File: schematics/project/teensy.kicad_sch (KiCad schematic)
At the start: 1 part

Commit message: First steps with kicad structure -> kinda sucks
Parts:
- added D? (x2): US1G, Diode_SMD:D_SMA, symbol Diode:US1G
- gave numbers to parts that had none: 1
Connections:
- net GND: now reaches U1.1 (GND)
- net GND: now also U1.64 (GND)
- net CS: now reaches U1.12 (10_CS_MQSR)
- net MOSI: now reaches U1.13 (11_MOSI_CTX1)
- net MISO: now reaches U1.14 (12_MISO_MQSL)
- net SCK: now reaches U1.35 (13_SCK_LED)
- net IRQ: now reaches U1.4 (2_OUT2)
- net SDA: now reaches U1.40 (18_A4_SDA)
- net SCL: now reaches U1.41 (19_A5_SCL)
- net +3V3: now reaches U1.46 (3V3)
- net +5P: now reaches U1.48 (VIN)
- net +5P: now also D?.2 (A)
- net +5F: now reaches U1.49 (VUSB)
- net +5F: now also D?.2 (A)
- new net +5V: D?.1 (K), D?.1 (K)
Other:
- note added: "IRQ geht auf OUT2????"
- note added: "MEM_CS von prop shield geht auf OUT1D???"

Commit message: some progress, dust slowly clears
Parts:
- removed D? (x2): US1G, Diode_SMD:D_SMA, symbol Diode:US1G
- added D1, D2: PMEG40T20ER, Diode_SMD:Nexperia_CFP3_SOD-123W, symbol Diode:PMEG40T20ER
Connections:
- net +5F: now also D1.2 (A)
- net +5P: now also D2.2 (A)
- net +5V: now also D1.1 (K), D2.1 (K)
- net footpad_a : now reaches U1.36 (14_A0_TX3_SPDIF_OUT)
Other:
- note added: "USB"

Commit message: small progress, angsthasen
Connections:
- net +3V3: now also U1.15 (3V3)
- net GND: now also U1.34 (GND), U1.47 (GND), U1.52 (GND), U1.58 (GND), U1.59 (GND)
- no-connect marks 0 -> 2

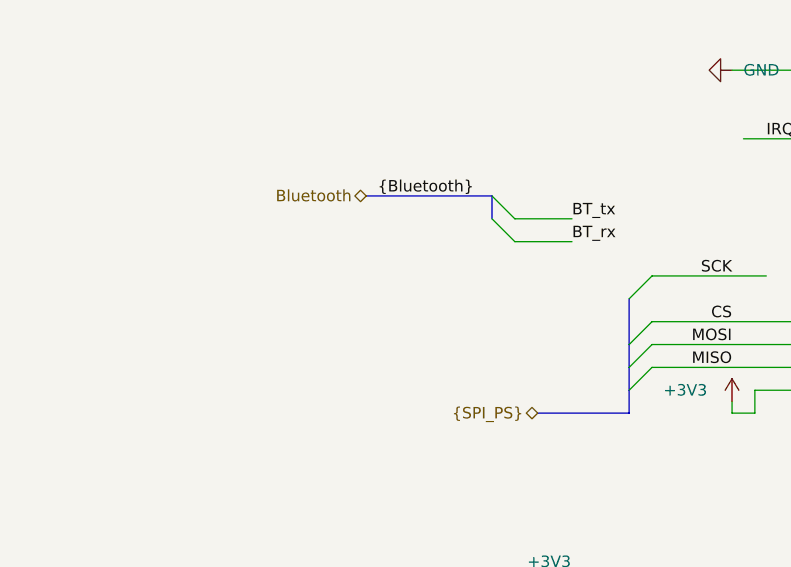
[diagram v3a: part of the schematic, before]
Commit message: Adding separate library, BT Module
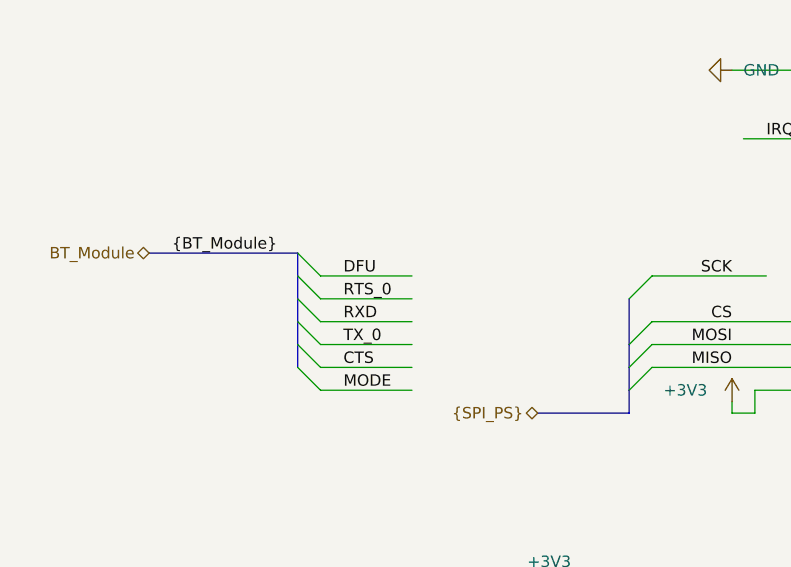
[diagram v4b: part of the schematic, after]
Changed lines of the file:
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@@
     (stroke (width 0) (type default) (color 0 0 0 0))
   )
-  (bus_entry (at 73.66 72.39) (size 2.54 2.54)
+  (bus_entry (at 52.07 86.36) (size 2.54 2.54)
     (stroke (width 0) (type default) (color 0 0 0 0))
   )
@@
     (stroke (width 0) (type default) (color 0 0 0 0))
   )
+  (bus_entry (at 52.07 83.82) (size 2.54 2.54)
+    (stroke (width 0) (type default) (color 0 0 0 0))
+  )
   (bus_entry (at 53.34 115.57) (size 2.54 2.54)
     (stroke (width 0) (type default) (color 0 0 0 0))
   )
+  (bus_entry (at 52.07 88.9) (size 2.54 2.54)
+    (stroke (width 0) (type default) (color 0 0 0 0))
+  )
+  (bus_entry (at 52.07 81.28) (size 2.54 2.54)
+    (stroke (width 0) (type default) (color 0 0 0 0))
+  )
+  (bus_entry (at 52.07 76.2) (size 2.54 2.54)
+    (stroke (width 0) (type default) (color 0 0 0 0))
+  )
   (bus_entry (at 46.99 137.16) (size 2.54 2.54)
     (stroke (width 0) (type default) (color 0 0 0 0))
@@
     (stroke (width 0) (type default) (color 0 0 0 0))
   )
+  (bus_entry (at 52.07 78.74) (size 2.54 2.54)
+    (stroke (width 0) (type default) (color 0 0 0 0))
+  )
   (bus_entry (at 195.58 71.12) (size 2.54 -2.54)
     (stroke (width 0) (type default) (color 0 0 0 0))
@@
     (stroke (width 0) (type default) (color 0 0 0 0))
   )
-  (bus_entry (at 73.66 69.85) (size 2.54 2.54)
-    (stroke (width 0) (type default) (color 0 0 0 0))
-  )
   (bus_entry (at 91.44 78.74) (size -2.54 2.54)
     (stroke (width 0) (type default) (color 0 0 0 0))
@@
     (stroke (width 0) (type default) (color 0 0 0 0))
   )
+  (wire (pts (xy 54.61 81.28) (xy 64.77 81.28))
+    (stroke (width 0) (type default) (color 0 0 0 0))
+  )
   (wire (pts (xy 139.7 143.51) (xy 139.7 146.05))
     (stroke (width 0) (type default) (color 0 0 0 0))
@@
     (stroke (width 0) (type default) (color 0 0 0 0))
   )
-  (wire (pts (xy 76.2 72.39) (xy 82.55 72.39))
+  (bus (pts (xy 52.07 83.82) (xy 52.07 86.36))
     (stroke (width 0) (type default) (color 0 0 0 0))
   )
@@
     (stroke (width 0) (type default) (color 0 0 0 0))
   )
+  (wire (pts (xy 54.61 78.74) (xy 64.77 78.74))
+    (stroke (width 0) (type default) (color 0 0 0 0))
+  )
   (wire (pts (xy 167.64 36.83) (xy 172.72 36.83))
     (stroke (width 0) (type default) (color 0 0 0 0))
@@
     (stroke (width 0) (type default) (color 0 0 0 0))
   )
+  (bus (pts (xy 52.07 76.2) (xy 52.07 78.74))
+    (stroke (width 0) (type default) (color 0 0 0 0))
+  )
   (bus (pts (xy 34.29 137.16) (xy 46.99 137.16))
     (stroke (width 0) (type default) (color 0 0 0 0))
@@
     (stroke (width 0) (type default) (color 0 0 0 0))
   )
+  (wire (pts (xy 54.61 86.36) (xy 64.77 86.36))
+    (stroke (width 0) (type default) (color 0 0 0 0))
+  )
   (wire (pts (xy 102.87 93.98) (xy 100.33 93.98))
     (stroke (width 0) (type default) (color 0 0 0 0))
@@
     (stroke (width 0) (type default) (color 0 0 0 0))
   )
-  (wire (pts (xy 76.2 74.93) (xy 82.55 74.93))
+  (wire (pts (xy 54.61 91.44) (xy 64.77 91.44))
+    (stroke (width 0) (type default) (color 0 0 0 0))
+  )
+  (wire (pts (xy 54.61 83.82) (xy 64.77 83.82))
     (stroke (width 0) (type default) (color 0 0 0 0))
   )
@@
     (stroke (width 0) (type default) (color 0 0 0 0))
   )
+  (bus (pts (xy 52.07 86.36) (xy 52.07 88.9))
+    (stroke (width 0) (type default) (color 0 0 0 0))
+  )
+  (bus (pts (xy 35.56 76.2) (xy 52.07 76.2))
+    (stroke (width 0) (type default) (color 0 0 0 0))
+  )
   (wire (pts (xy 236.22 52.07) (xy 242.57 52.07))
     (stroke (width 0) (type default) (color 0 0 0 0))
@@
     (stroke (width 0) (type default) (color 0 0 0 0))
   )
+  (bus (pts (xy 52.07 81.28) (xy 52.07 83.82))
+    (stroke (width 0) (type default) (color 0 0 0 0))
+  )
   (wire (pts (xy 167.64 52.07) (xy 170.18 52.07))
     (stroke (width 0) (type default) (color 0 0 0 0))
@@
     (stroke (width 0) (type default) (color 0 0 0 0))
   )
-  (bus (pts (xy 73.66 69.85) (xy 73.66 72.39))
-    (stroke (width 0) (type default) (color 0 0 0 0))
-  )
   (wire (pts (xy 55.88 118.11) (xy 64.77 118.11))
     (stroke (width 0) (type default) (color 0 0 0 0))
@@
     (stroke (width 0) (type default) (color 0 0 0 0))
   )
+  (wire (pts (xy 54.61 88.9) (xy 64.77 88.9))
+    (stroke (width 0) (type default) (color 0 0 0 0))
+  )
   (wire (pts (xy 172.72 26.67) (xy 172.72 24.13))
     (stroke (width 0) (type default) (color 0 0 0 0))
@@
     (stroke (width 0) (type default) (color 0 0 0 0))
   )
+  (bus (pts (xy 52.07 78.74) (xy 52.07 81.28))
+    (stroke (width 0) (type default) (color 0 0 0 0))
+  )
   (wire (pts (xy 173.99 91.44) (xy 173.99 93.98))
     (stroke (width 0) (type default) (color 0 0 0 0))
@@
     (stroke (width 0) (type default) (color 0 0 0 0))
   )
-  (bus (pts (xy 59.69 69.85) (xy 73.66 69.85))
-    (stroke (width 0) (type default) (color 0 0 0 0))
-  )
   (wire (pts (xy 102.87 91.44) (xy 102.87 93.98))
     (stroke (width 0) (type default) (color 0 0 0 0))
@@
     (effects (font (size 1.27 1.27)) (justify left bottom))
   )
-  (label "BT_tx" (at 82.55 72.39 0)
+  (label "RTS_0" (at 57.15 81.28 0)
+    (effects (font (size 1.27 1.27)) (justify left bottom))
+  )
+  (label "CTS" (at 57.15 88.9 0)
     (effects (font (size 1.27 1.27)) (justify left bottom))
   )
@@
   )
   (label "RS485_A" (at 204.47 118.11 0)
+    (effects (font (size 1.27 1.27)) (justify left bottom))
+  )
+  (label "{BT_Module}" (at 38.1 76.2 0)
     (effects (font (size 1.27 1.27)) (justify left bottom))
   )
@@
     (effects (font (size 1.27 1.27)) (justify left bottom))
   )
+  (label "DFU" (at 57.15 78.74 0)
+    (effects (font (size 1.27 1.27)) (justify left bottom))
+  )
   (label "CS" (at 100.33 83.82 180)
     (effects (font (size 1.27 1.27)) (justify right bottom))
   )
+  (label "RXD" (at 57.15 83.82 0)
+    (effects (font (size 1.27 1.27)) (justify left bottom))
+  )
   (label "{Hall}" (at 39.37 113.03 0)
     (effects (font (size 1.27 1.27)) (justify left bottom))
@@
   )
   (label "{poti_IN}" (at 36.83 137.16 0)
-    (effects (font (size 1.27 1.27)) (justify left bottom))
-  )
-  (label "BT_rx" (at 82.55 74.93 0)
     (effects (font (size 1.27 1.27)) (justify left bottom))
   )
@@
     (effects (font (size 1.27 1.27)) (justify right bottom))
   )
-  (label "{Bluetooth}" (at 60.96 69.85 0)
+  (label "TX_0" (at 57.15 86.36 0)
+    (effects (font (size 1.27 1.27)) (justify left bottom))
+  )
+  (label "MODE" (at 57.15 91.44 0)
     (effects (font (size 1.27 1.27)) (justify left bottom))
   )
@@
     (effects (font (size 1.27 1.27)) (justify right))
   )
+  (hierarchical_label "BT_Module" (shape bidirectional) (at 35.56 76.2 180)
+    (effects (font (size 1.27 1.27)) (justify right))
+  )
   (hierarchical_label "speed_slow" (shape output) (at 35.56 39.37 180)
     (effects (font (size 1.27 1.27)) (justify right))
@@
     (effects (font (size 1.27 1.27)) (justify left))
   )
-  (hierarchical_label "Bluetooth" (shape bidirectional) (at 59.69 69.85 180)
-    (effects (font (size 1.27 1.27)) (justify right))
-  )
   (symbol (lib_id "power:+5V") (at 172.72 24.13 0) (unit 1)

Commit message: random commit
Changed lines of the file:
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@@
   (paper "A4")
   (bus_alias "analog_reserve" (members ))
+  (bus_alias "digital_reserve" (members "d1" "d0" "d2"))
   (junction (at 172.72 26.67) (diameter 0) (color 0 0 0 0)
   )
@@
     (stroke (width 0) (type default) (color 0 0 0 0))
   )
-  (bus_entry (at 245.11 49.53) (size -2.54 2.54)
-    (stroke (width 0) (type default) (color 0 0 0 0))
-  )
-  (bus_entry (at 245.11 52.07) (size -2.54 2.54)
-    (stroke (width 0) (type default) (color 0 0 0 0))
-  )
-  (bus_entry (at 245.11 54.61) (size -2.54 2.54)
+  (bus_entry (at 237.49 49.53) (size -2.54 2.54)
+    (stroke (width 0) (type default) (color 0 0 0 0))
+  )
+  (bus_entry (at 237.49 52.07) (size -2.54 2.54)
+    (stroke (width 0) (type default) (color 0 0 0 0))
+  )
+  (bus_entry (at 237.49 54.61) (size -2.54 2.54)
+    (stroke (width 0) (type default) (color 0 0 0 0))
+  )
+  (bus_entry (at 238.76 68.58) (size -2.54 2.54)
     (stroke (width 0) (type default) (color 0 0 0 0))
   )
@@
     (stroke (width 0) (type default) (color 0 0 0 0))
   )
+  (bus_entry (at 238.76 71.12) (size -2.54 2.54)
+    (stroke (width 0) (type default) (color 0 0 0 0))
+  )
+  (bus_entry (at 238.76 66.04) (size -2.54 2.54)
+    (stroke (width 0) (type default) (color 0 0 0 0))
+  )
   (bus_entry (at 91.44 78.74) (size -2.54 2.54)
     (stroke (width 0) (type default) (color 0 0 0 0))
@@
     (stroke (width 0) (type default) (color 0 0 0 0))
   )
-  (bus (pts (xy 245.11 52.07) (xy 245.11 54.61))
+  (bus (pts (xy 237.49 52.07) (xy 237.49 54.61))
     (stroke (width 0) (type default) (color 0 0 0 0))
   )
@@
     (stroke (width 0) (type default) (color 0 0 0 0))
   )
+  (wire (pts (xy 228.6 68.58) (xy 236.22 68.58))
+    (stroke (width 0) (type default) (color 0 0 0 0))
+  )
   (wire (pts (xy 204.47 120.65) (xy 223.52 120.65))
     (stroke (width 0) (type default) (color 0 0 0 0))
@@
     (stroke (width 0) (type default) (color 0 0 0 0))
   )
+  (bus (pts (xy 238.76 66.04) (xy 257.81 66.04))
+    (stroke (width 0) (type default) (color 0 0 0 0))
+  )
   (wire (pts (xy 102.87 93.98) (xy 100.33 93.98))
     (stroke (width 0) (type default) (color 0 0 0 0))
@@
     (stroke (width 0) (type default) (color 0 0 0 0))
   )
-  (wire (pts (xy 236.22 52.07) (xy 242.57 52.07))
+  (wire (pts (xy 228.6 52.07) (xy 234.95 52.07))
     (stroke (width 0) (type default) (color 0 0 0 0))
   )
@@
     (stroke (width 0) (type default) (color 0 0 0 0))
   )
+  (wire (pts (xy 228.6 71.12) (xy 236.22 71.12))
+    (stroke (width 0) (type default) (color 0 0 0 0))
+  )
   (wire (pts (xy 55.88 118.11) (xy 64.77 118.11))
     (stroke (width 0) (type default) (color 0 0 0 0))
@@
     (stroke (width 0) (type default) (color 0 0 0 0))
   )
-  (wire (pts (xy 236.22 54.61) (xy 242.57 54.61))
+  (wire (pts (xy 228.6 54.61) (xy 234.95 54.61))
     (stroke (width 0) (type default) (color 0 0 0 0))
   )
@@
     (stroke (width 0) (type default) (color 0 0 0 0))
   )
+  (bus (pts (xy 238.76 68.58) (xy 238.76 71.12))
+    (stroke (width 0) (type default) (color 0 0 0 0))
+  )
   (wire (pts (xy 55.88 115.57) (xy 64.77 115.57))
     (stroke (width 0) (type default) (color 0 0 0 0))
@@
     (stroke (width 0) (type default) (color 0 0 0 0))
   )
+  (wire (pts (xy 228.6 73.66) (xy 236.22 73.66))
+    (stroke (width 0) (type default) (color 0 0 0 0))
+  )
   (wire (pts (xy 167.64 123.19) (xy 173.99 123.19))
     (stroke (width 0) (type default) (color 0 0 0 0))
@@
     (stroke (width 0) (type default) (color 0 0 0 0))
   )
-  (wire (pts (xy 236.22 57.15) (xy 242.57 57.15))
+  (wire (pts (xy 228.6 57.15) (xy 234.95 57.15))
     (stroke (width 0) (type default) (color 0 0 0 0))
   )
@@
     (stroke (width 0) (type default) (color 0 0 0 0))
   )
-  (bus (pts (xy 245.11 49.53) (xy 245.11 52.07))
+  (bus (pts (xy 238.76 66.04) (xy 238.76 68.58))
+    (stroke (width 0) (type default) (color 0 0 0 0))
+  )
+  (bus (pts (xy 237.49 49.53) (xy 237.49 52.07))
     (stroke (width 0) (type default) (color 0 0 0 0))
   )
@@
     (stroke (width 0) (type default) (color 0 0 0 0))
   )
-  (bus (pts (xy 245.11 49.53) (xy 265.43 49.53))
+  (bus (pts (xy 237.49 49.53) (xy 257.81 49.53))
     (stroke (width 0) (type default) (color 0 0 0 0))
   )
@@
     (effects (font (size 1.27 1.27)) (justify left bottom))
   )
+  (label "d2" (at 228.6 73.66 0)
+    (effects (font (size 1.27 1.27)) (justify left bottom))
+  )
   (label "RTS_0" (at 57.15 81.28 0)
     (effects (font (size 1.27 1.27)) (justify left bottom))
@@
     (effects (font (size 1.27 1.27)) (justify left bottom))
   )
+  (label "d1" (at 228.6 71.12 0)
+    (effects (font (size 1.27 1.27)) (justify left bottom))
+  )
   (label "poti_IN_a0" (at 49.53 139.7 0)
     (effects (font (size 1.27 1.27)) (justify left bottom))
   )
-  (label "a1" (at 237.49 54.61 0)
+  (label "{digital_reserve}" (at 241.3 66.04 0)
+    (effects (font (size 1.27 1.27)) (justify left bottom))
+  )
+  (label "a1" (at 229.87 54.61 0)
     (effects (font (size 1.27 1.27)) (justify left bottom))
   )
@@
     (effects (font (size 1.27 1.27)) (justify left bottom))
   )
-  (label "a2" (at 237.49 57.15 0)
-    (effects (font (size 1.27 1.27)) (justify left bottom))
-  )
-  (label "a0" (at 237.49 52.07 0)
+  (label "a2" (at 229.87 57.15 0)
+    (effects (font (size 1.27 1.27)) (justify left bottom))
+  )
+  (label "a0" (at 229.87 52.07 0)
     (effects (font (size 1.27 1.27)) (justify left bottom))
   )
@@
     (effects (font (size 1.27 1.27)) (justify left bottom))
   )
-  (label "{analog_reserve}" (at 247.65 49.53 0)
+  (label "{analog_reserve}" (at 240.03 49.53 0)
     (effects (font (size 1.27 1.27)) (justify left bottom))
   )
   (label "{poti_IN}" (at 36.83 137.16 0)
+    (effects (font (size 1.27 1.27)) (justify left bottom))
+  )
+  (label "d0" (at 228.6 68.58 0)
     (effects (font (size 1.27 1.27)) (justify left bottom))
   )
@@
     (effects (font (size 1.27 1.27)) (justify right))
   )
+  (hierarchical_label "analog_reserve" (shape bidirectional) (at 257.81 49.53 0)
+    (effects (font (size 1.27 1.27)) (justify left))
+  )
   (hierarchical_label "speed_slow" (shape output) (at 35.56 39.37 180)
     (effects (font (size 1.27 1.27)) (justify right))
@@
     (effects (font (size 1.27 1.27)) (justify right))
   )
+  (hierarchical_label "digital_reserve" (shape bidirectional) (at 257.81 66.04 0)
+    (effects (font (size 1.27 1.27)) (justify left))
+  )
   (hierarchical_label "RS485_BMS" (shape bidirectional) (at 243.84 115.57 0)
